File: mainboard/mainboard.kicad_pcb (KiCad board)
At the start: 2 copper layers, 80 x 100 mm, 68 parts, among them J1 Eurorack_Power, J2 Osc1_Socket, J3 Osc2_Socket, Q1 2N3906, Q2 2N3906, Q3 2N3904, Q4 2N3904, U1 40106, U2 TL074, U4 4070, U5 4520, U6 4015, U7 4015

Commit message: Routing done, panel done
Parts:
- moved C9 29.1 mm to (38.8, 52.8), turned to 0 degrees
- moved C1 24.1 mm to (51.5, 33.2), turned to -90 degrees
- moved R1 23.5 mm to (34.2, 2.69), turned to -90 degrees
- moved C4 23.4 mm to (28.5, 35.5)
- moved R2 23.3 mm to (46.5, 2.69), turned to -90 degrees
- moved U1 22.7 mm to (43.8, 49.4), turned to 180 degrees
- moved D4 21.4 mm to (48.0, 49.3), turned to 90 degrees
- moved D3 21.4 mm to (32.0, 49.4), turned to 90 degrees
- moved R7 21.2 mm to (36.2, 30.8), turned to 0 degrees
- moved R5 19.8 mm to (46.0, 16.4), turned to -90 degrees
- moved R8 19.3 mm to (36.2, 28.0), turned to 0 degrees
- moved C7 16.6 mm to (28.0, 80.8), turned to -90 degrees
- moved R3 15.5 mm to (48.0, 38.6), turned to 90 degrees
- moved R6 15.5 mm to (32.0, 38.4), turned to 90 degrees
- moved C5 14.1 mm to (28.5, 44.2)
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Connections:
- J2 pad 3: Rst1 -> unconnected-(J2-Pad3)
- J2 pad 4: D1 -> RM
- J2 pad 5: unconnected-(J2-Pad5) -> D1
- J2 pad 6: RM -> Osc1
- J2 pad 7: Osc1 -> Rst1
- J3 pad 10: Sin2 -> Rung2
- J3 pad 11: Rung2 -> Sin2
- J3 pad 3: Rst2 -> Osc3sw
- J3 pad 5: Osc3sw -> Osc2
- J3 pad 7: Osc2 -> Clk2
- J3 pad 8: Clk2 -> QB8
- J3 pad 9: QB8 -> Rst2
- U1 pad 1: Net-(C5-Pad2) -> Net-(C6-Pad2)
- U1 pad 10: O2 -> O1
- U1 pad 11: Net-(D4-Pad2) -> Net-(D3-Pad2)
- U1 pad 12: Net-(D4-Pad2) -> Net-(D3-Pad2)
- U1 pad 13: Net-(C6-Pad2) -> Net-(C5-Pad2)
- U1 pad 2: Net-(D3-Pad2) -> Net-(D4-Pad2)
- U1 pad 3: Net-(D3-Pad2) -> Net-(D4-Pad2)
- U1 pad 4: O1 -> O2
- U4 pad 1: Osc1 -> Osc2
- U4 pad 2: Osc2 -> Osc1
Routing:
- net 12v: track 0.00 -> 303.7 mm
- net -12v: track 0.00 -> 134.2 mm
- net QA8: track 0.00 -> 132.3 mm
- net QB8: track 0.00 -> 121.2 mm
- net GND: track 0.00 -> 105.7 mm, vias 0 -> 2
- net Osc2: track 0.00 -> 101.0 mm
- net Osc1: track 0.00 -> 97.4 mm
- net Net-(U4-Pad10): track 0.00 -> 94.5 mm
- net D1: track 0.00 -> 82.7 mm
- net RM: track 0.00 -> 69.3 mm
- net Net-(U4-Pad11): track 0.00 -> 67.1 mm
- net Net-(R17-Pad2): track 0.00 -> 56.6 mm
- net O1: track 0.00 -> 51.6 mm, vias 0 -> 1
- net QB6: track 0.00 -> 51.0 mm
- net QB7: track 0.00 -> 50.6 mm
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- added copper zone on B.Cu, net GND
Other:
- outline, holes or cut-outs redrawn

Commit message: Updates to panel etc.
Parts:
- moved R25 0.75 mm to (22.1, 97.2)
- moved R13 0.25 mm to (22.1, 94.5)
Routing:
- net Net-(R10-Pad2): track 44.2 -> 43.4 mm
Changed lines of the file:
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@@
   )
   (footprint "Resistor_THT:R_Axial_DIN0204_L3.6mm_D1.6mm_P7.62mm_Horizontal" (layer "F.Cu")
-    (at 22.06 98 180)
+    (at 22.06 97.25 180)
     (descr "Resistor, Axial_DIN0204 series, Axial, Horizontal, pin pitch=7.62mm, 0.167W, length*diameter=3.6*1.6mm^2, http://cdn-reichelt.de/documents/datenblatt/B400/1_4W%23YAG.pdf")
     (tags "Resistor Axial_DIN0204 series Axial Horizontal pin pitch 7.62mm 0.167W length 3.6mm diameter 1.6mm")
@@
   )
   (footprint "Resistor_THT:R_Axial_DIN0204_L3.6mm_D1.6mm_P7.62mm_Horizontal" (layer "F.Cu")
-    (at 22.06 94.25 180)
+    (at 22.06 94.5 180)
     (descr "Resistor, Axial_DIN0204 series, Axial, Horizontal, pin pitch=7.62mm, 0.167W, length*diameter=3.6*1.6mm^2, http://cdn-reichelt.de/documents/datenblatt/B400/1_4W%23YAG.pdf")
     (tags "Resistor Axial_DIN0204 series Axial Horizontal pin pitch 7.62mm 0.167W length 3.6mm diameter 1.6mm")
@@
   (segment (start 22.06 83.5) (end 22.06 80.75) (width 0.25) (layer "B.Cu") (net 37))
   (segment (start 22.06 80.75) (end 22.06 78) (width 0.25) (layer "B.Cu") (net 37))
+  (segment (start 14.44 94.5) (end 14.44 91.75) (width 0.25) (layer "B.Cu") (net 37))
   (segment (start 14.44 89) (end 14.44 86.25) (width 0.25) (layer "B.Cu") (net 37))
   (segment (start 14.44 91.75) (end 14.44 89) (width 0.25) (layer "B.Cu") (net 37))
-  (segment (start 14.44 94.25) (end 14.44 91.75) (width 0.25) (layer "B.Cu") (net 37))
-  (segment (start 14.44 98) (end 14.44 94.25) (width 0.25) (layer "B.Cu") (net 37))
+  (segment (start 14.44 97.25) (end 14.44 94.5) (width 0.25) (layer "B.Cu") (net 37))
   (segment (start 11.75 64.12) (end 11.75 75.31) (width 0.25) (layer "B.Cu") (net 38))
   (segment (start 14.5 61.37) (end 11.75 64.12) (width 0.25) (layer "B.Cu") (net 38))
@@
   (segment (start 74.75 20.85) (end 74.75 26.25) (width 0.25) (layer "F.Cu") (net 67))
   (segment (start 57.141422 35.25) (end 55.299511 37.091911) (width 0.25) (layer "F.Cu") (net 67))
+  (segment (start 25.501489 93.730134) (end 25.501489 84.079916) (width 1) (layer "F.Cu") (net 68))
   (segment (start 36.75 56) (end 38 56) (width 1) (layer "F.Cu") (net 68))
+  (segment (start 22.06 97.25) (end 22.81 97.25) (width 1) (layer "F.Cu") (net 68))
   (segment (start 41.25 36.5) (end 43.615 34.135) (width 1) (layer "F.Cu") (net 68))
-  (segment (start 25.5 93.731573) (end 25.5 84.078427) (width 1) (layer "F.Cu") (net 68))
-  (segment (start 26.085787 82.664213) (end 28 80.75) (width 1) (layer "F.Cu") (net 68))
   (segment (start 28 80.75) (end 33.75 80.75) (width 1) (layer "F.Cu") (net 68))
+  (segment (start 25.501489 84.079916) (end 25.5 84.078427) (width 1) (layer "F.Cu") (net 68))
   (segment (start 63.5 25.25) (end 57.500002 31.25) (width 1) (layer "F.Cu") (net 68))
   (segment (start 43.615 34.135) (end 43.8 34.135) (width 1) (layer "F.Cu") (net 68))
   (segment (start 63.5 25.24) (end 66.5 22.24) (width 1) (layer "F.Cu") (net 68))
+  (segment (start 22.81 97.25) (end 24.914214 95.145786) (width 1) (layer "F.Cu") (net 68))
   (segment (start 38 56) (end 41.25 52.75) (width 1) (layer "F.Cu") (net 68))
   (segment (start 66.5 22.24) (end 66.5 6.5) (width 1) (layer "F.Cu") (net 68))
   (segment (start 63.5 25.24) (end 63.5 25.25) (width 1) (layer "F.Cu") (net 68))
   (segment (start 28.5 44.25) (end 28.5 35.5) (width 1) (layer "F.Cu") (net 68))
+  (segment (start 25.5 93.731623) (end 25.501489 93.730134) (width 1) (layer "F.Cu") (net 68))
   (segment (start 33.75 80.75) (end 34 81) (width 1) (layer "F.Cu") (net 68))
-  (segment (start 22.06 98) (end 24.914214 95.145786) (width 1) (layer "F.Cu") (net 68))
   (segment (start 41.25 52.75) (end 41.25 36.5) (width 1) (layer "F.Cu") (net 68))
+  (segment (start 26.085787 82.664213) (end 28 80.75) (width 1) (layer "F.Cu") (net 68))
   (via (at 57.500002 31.25) (size 0.8) (drill 0.4) (layers "F.Cu" "B.Cu") (free) (net 68))
   (via (at 36.75 56) (size 0.8) (drill 0.4) (layers "F.Cu" "B.Cu") (free) (net 68))
-  (arc (start 25.5 93.731573) (mid 25.347759 94.49694) (end 24.914214 95.145786) (width 1) (layer "F.Cu") (net 68))
   (arc (start 25.5 84.078427) (mid 25.652241 83.31306) (end 26.085787 82.664213) (width 1) (layer "F.Cu") (net 68))
+  (arc (start 24.914214 95.145786) (mid 25.34776 94.496966) (end 25.5 93.731623) (width 1) (layer "F.Cu") (net 68))
   (segment (start 46 81) (end 51.75 81) (width 1) (layer "B.Cu") (net 68))
   (segment (start 14.5 71.53) (end 14.72 71.53) (width 1) (layer "B.Cu") (net 68))

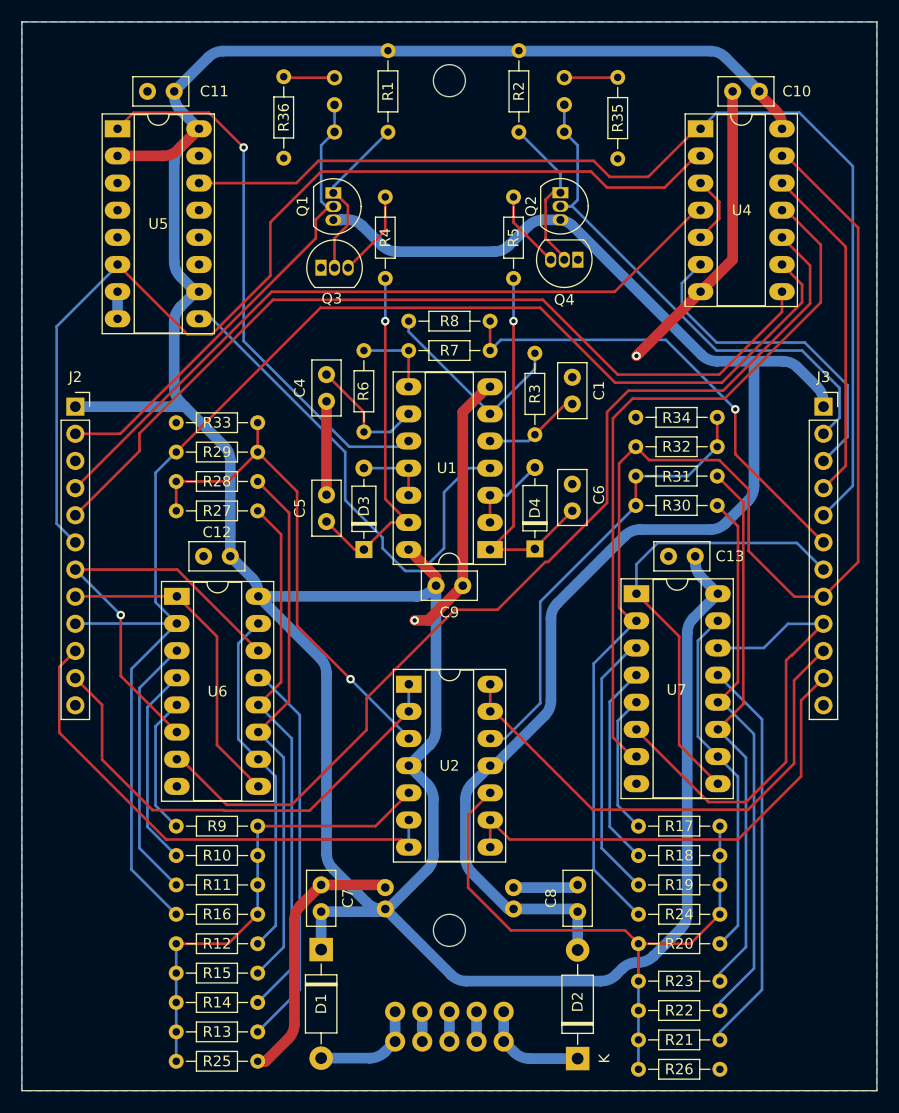
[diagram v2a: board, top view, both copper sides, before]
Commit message: Removed the unneccessary 100ohm resistor after the expo converter
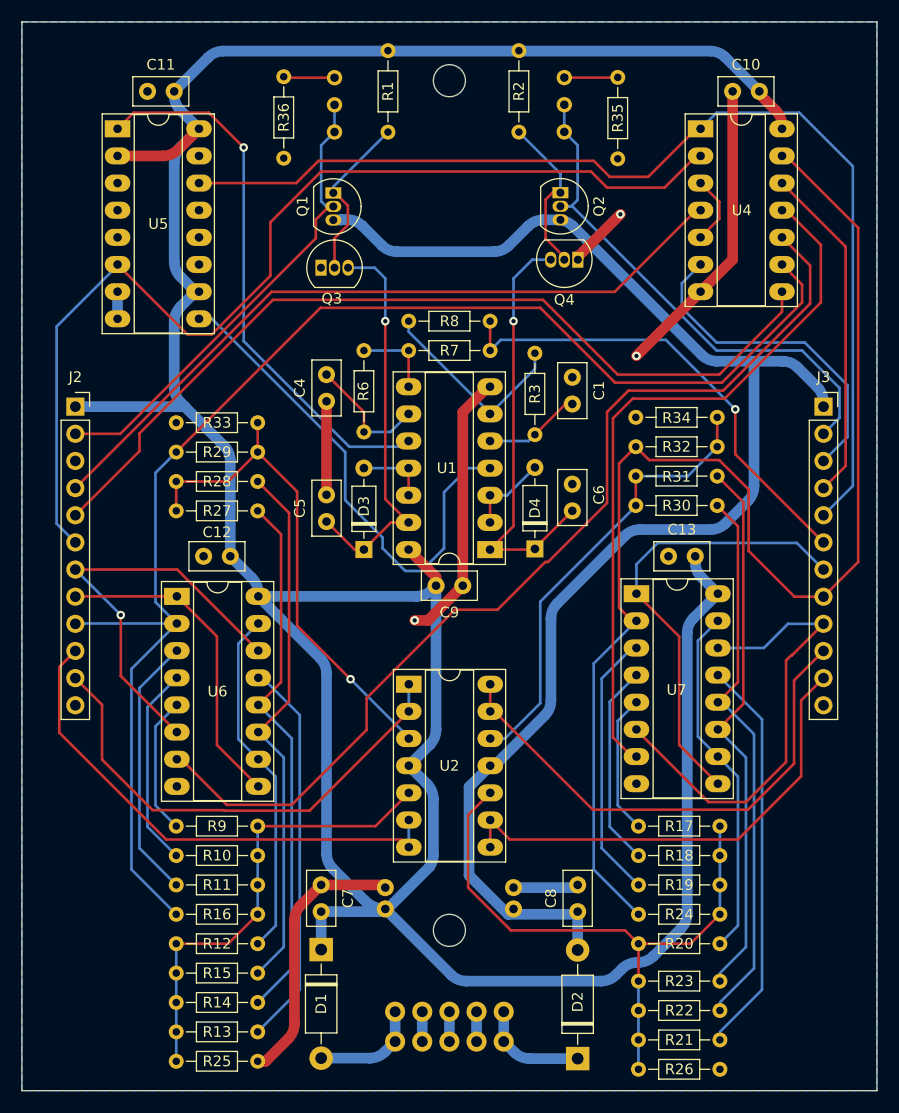
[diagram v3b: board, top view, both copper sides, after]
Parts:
- removed R4, R5: 100, Resistor_THT:R_Axial_DIN0204_L3.6mm_D1.6mm_P7.62mm_Horizontal
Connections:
- Q3 pad 3: Net-(Q3-Pad3) -> Net-(C5-Pad2)
- Q4 pad 3: Net-(Q4-Pad3) -> Net-(C6-Pad2)
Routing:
- net Net-(Q3-Pad3): track 8.06 -> 0.00 mm
- net Net-(Q4-Pad3): track 7.19 -> 0.00 mm
- net GND: track 105.4 -> 111.3 mm, vias 2 -> 3
- net Net-(C6-Pad2): track 35.5 -> 39.7 mm
- net Net-(C5-Pad2): track 33.6 -> 37.4 mm
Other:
- board text added: "Dual Digital Sine Wave Generator Design and PCB by Neil Massey CC-BY-NC-SA 3.0 (2022) Rev 0"
- board text removed: "+"
- board text removed: "Design and PCB by Neil Massey CC-BY-NC-SA 3.0 (2022) Rev 0"
- board text removed: "Dual Digital Sine Wave Generator"

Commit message: Added range switch
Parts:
- removed C5: 10nF, Capacitor_THT:C_Disc_D5.0mm_W2.5mm_P2.50mm
- removed C6: 10nf, Capacitor_THT:C_Disc_D5.0mm_W2.5mm_P2.50mm
- R1, R2: value 2.2M -> 1M
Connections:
- D3 pad 1: Net-(C5-Pad2) -> RATESEL1
- D4 pad 1: Net-(C6-Pad2) -> RATESEL2
- J2 pad 3: unconnected-(J2-Pad3) -> RATESEL1
- J3 pad 10: Rung2 -> Rst2
- J3 pad 11: Sin2 -> Rung2
- J3 pad 12: GND -> Sin2
- J3 pad 3: Osc3sw -> RATESEL2
- J3 pad 4: D2 -> Osc3sw
- J3 pad 5: Osc2 -> D2
- J3 pad 6: Osc3 -> Osc2
- J3 pad 7: Clk2 -> Osc3
- J3 pad 8: QB8 -> Clk2
- J3 pad 9: Rst2 -> QB8
- Q3 pad 3: Net-(C5-Pad2) -> RATESEL1
- Q4 pad 3: Net-(C6-Pad2) -> RATESEL2
- U1 pad 1: Net-(C6-Pad2) -> RATESEL2
- U1 pad 13: Net-(C5-Pad2) -> RATESEL1
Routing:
- net RATESEL2: track 0.00 -> 68.5 mm, vias 0 -> 2
- net RATESEL1: track 0.00 -> 66.0 mm, vias 0 -> 2
- net Net-(C6-Pad2): track 39.7 -> 0.00 mm, vias 1 -> 0
- net Net-(C5-Pad2): track 37.4 -> 0.00 mm, vias 1 -> 0
- net GND: track 111.3 -> 102.6 mm
- net O2: track 47.3 -> 55.5 mm
- net QB8: track 121.2 -> 124.8 mm
- net Clk2: track 43.0 -> 40.0 mm
- net Rst2: track 43.7 -> 40.8 mm
- net Osc3: track 44.7 -> 47.4 mm
- net Osc2: track 101.0 -> 103.6 mm
- net Rung2: track 48.2 -> 45.7 mm
- net Sin2: track 44.9 -> 42.3 mm
- net D2: track 31.9 -> 34.4 mm
- net Osc3sw: track 31.3 -> 33.8 mm
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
